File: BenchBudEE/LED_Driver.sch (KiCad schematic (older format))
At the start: 6 parts

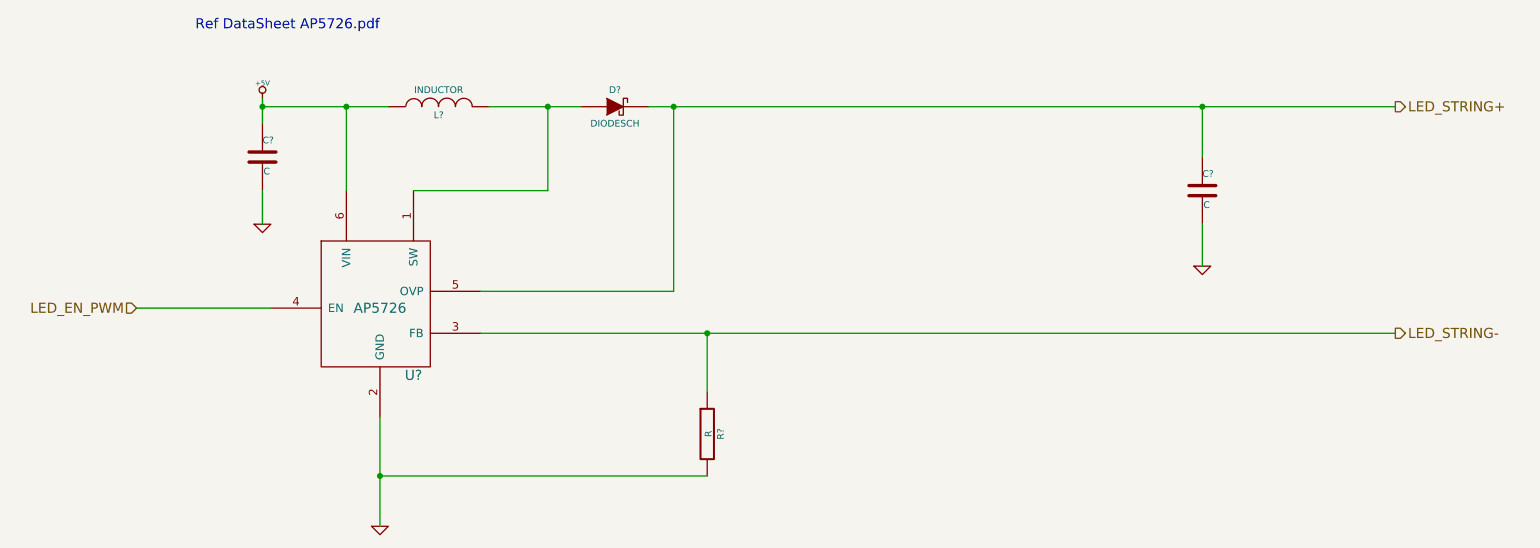
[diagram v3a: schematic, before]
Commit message: Placed the relay components.
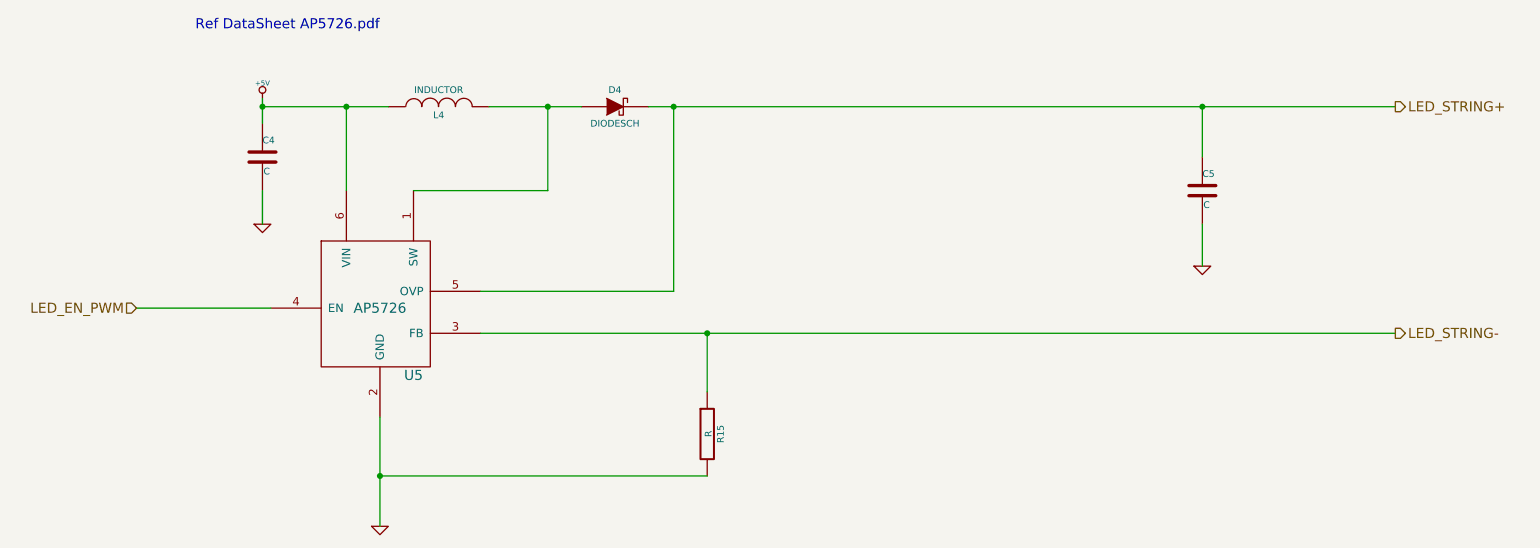
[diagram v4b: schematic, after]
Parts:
- gave numbers to parts that had none: 6
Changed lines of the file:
@@
 Sheet 6 9
 Title ""
-Date "19 feb 2014"
+Date "20 feb 2014"
 Rev ""
 Comp ""
@@
 LED_STRING-
 $Comp
-L AP5726 U?
+L AP5726 U5
 U 1 1 52F83C82
 P 3050 2300
-F 0 "U?" H 3250 1900 60  0000 C CNN
+F 0 "U5" H 3250 1900 60  0000 C CNN
 F 1 "AP5726" H 3050 2300 60  0000 C CNN
 F 2 "" H 3050 2300 60  0000 C CNN
@@
 	1600 2300 2400 2300
 $Comp
-L +5V #PWR?
+L +5V #PWR29
 U 1 1 52F8436F
 P 2350 1050
-F 0 "#PWR?" H 2350 1140 20  0001 C CNN
+F 0 "#PWR29" H 2350 1140 20  0001 C CNN
 F 1 "+5V" H 2350 1140 30  0000 C CNN
 F 2 "" H 2350 1050 60  0000 C CNN
@@
 $EndComp
 $Comp
-L GND #PWR?
+L GND #PWR30
 U 1 1 52F8437E
 P 2350 1800
-F 0 "#PWR?" H 2350 1800 30  0001 C CNN
+F 0 "#PWR30" H 2350 1800 30  0001 C CNN
 F 1 "GND" H 2350 1730 30  0001 C CNN
 F 2 "" H 2350 1800 60  0000 C CNN
@@
 $EndComp
 $Comp
-L GND #PWR?
+L GND #PWR31
 U 1 1 52F8438B
 P 3050 3600
-F 0 "#PWR?" H 3050 3600 30  0001 C CNN
+F 0 "#PWR31" H 3050 3600 30  0001 C CNN
 F 1 "GND" H 3050 3530 30  0001 C CNN
 F 2 "" H 3050 3600 60  0000 C CNN
@@
 	3050 2950 3050 3600
 $Comp
-L C C?
+L C C4
 U 1 1 52F84395
 P 2350 1400
-F 0 "C?" H 2350 1500 40  0000 L CNN
+F 0 "C4" H 2350 1500 40  0000 L CNN
 F 1 "C" H 2356 1315 40  0000 L CNN
 F 2 "~" H 2388 1250 30  0000 C CNN
@@
 Connection ~ 2350 1100
 $Comp
-L C C?
+L C C5
 U 1 1 52F845D8
 P 7950 1600
-F 0 "C?" H 7950 1700 40  0000 L CNN
+F 0 "C5" H 7950 1700 40  0000 L CNN
 F 1 "C" H 7956 1515 40  0000 L CNN
 F 2 "~" H 7988 1450 30  0000 C CNN
@@
 $EndComp
 $Comp
-L INDUCTOR L?
+L INDUCTOR L4
 U 1 1 52F845E0
 P 3400 1100
-F 0 "L?" V 3350 1100 40  0000 C CNN
+F 0 "L4" V 3350 1100 40  0000 C CNN
 F 1 "INDUCTOR" V 3500 1100 40  0000 C CNN
 F 2 "~" H 3400 1100 60  0000 C CNN
@@
 	4050 1600 3250 1600
 $Comp
-L DIODESCH D?
+L DIODESCH D4
 U 1 1 52F84602
 P 4450 1100
-F 0 "D?" H 4450 1200 40  0000 C CNN
+F 0 "D4" H 4450 1200 40  0000 C CNN
 F 1 "DIODESCH" H 4450 1000 40  0000 C CNN
 F 2 "~" H 4450 1100 60  0000 C CNN
@@
 Ref DataSheet AP5726.pdf
 $Comp
-L GND #PWR?
+L GND #PWR32
 U 1 1 52F84869
 P 7950 2050
-F 0 "#PWR?" H 7950 2050 30  0001 C CNN
+F 0 "#PWR32" H 7950 2050 30  0001 C CNN
 F 1 "GND" H 7950 1980 30  0001 C CNN
 F 2 "" H 7950 2050 60  0000 C CNN
@@
 Connection ~ 7950 1100
 $Comp
-L R R?
+L R R15
 U 1 1 52F84AC1
 P 5000 3050
-F 0 "R?" V 5080 3050 40  0000 C CNN
+F 0 "R15" V 5080 3050 40  0000 C CNN
 F 1 "R" V 5007 3051 40  0000 C CNN
 F 2 "~" V 4930 3050 30  0000 C CNN
